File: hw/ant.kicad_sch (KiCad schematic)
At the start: 0 parts

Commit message: Checkpoint
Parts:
- added J701: Conn_Coaxial_Power, Connector_Coaxial:SMA_Amphenol_132289_EdgeMount, symbol Connector:Conn_Coaxial_Power
- added K701: G5Q-1, Relay_THT:Relay_SPDT_Omron-G5Q-1, symbol Relay:G5Q-1
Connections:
- net AntRx: now also K701.4
- net AntTx: now also K701.3
- new net: J701.1 (In), K701.2
- new net GND: J701.2 (Ext), K701.5
- new net TxRelay: K701.1
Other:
- removed sheet BPF1
- removed sheet BPF10
- removed sheet BPF2
- removed sheet BPF3
- removed sheet BPF4
- removed sheet BPF5
- removed sheet BPF6
- removed sheet BPF7
- removed sheet BPF8
- removed sheet BPF9
- title: Antenna Tuner, BPF Array, Tx/Rx Relays -> Antenna Tuner, Tx/Rx Relays

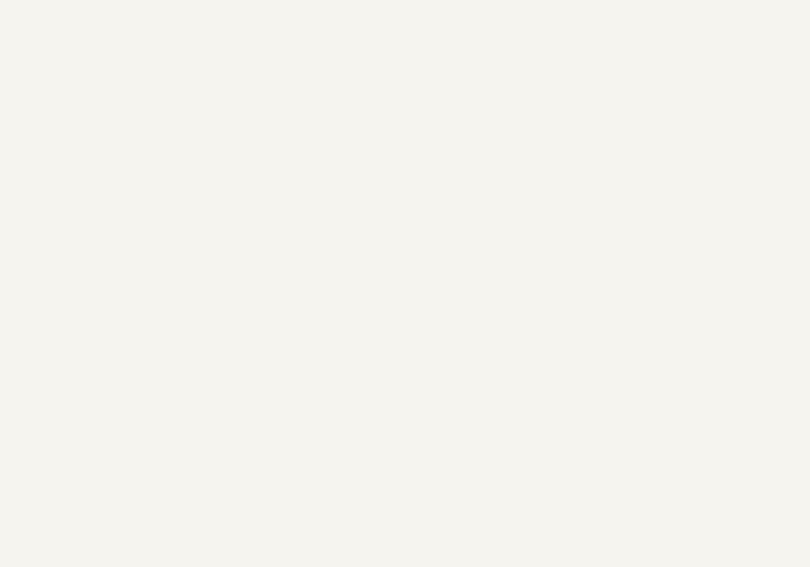
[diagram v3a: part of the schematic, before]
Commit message: Starting to switch to new rx architecture
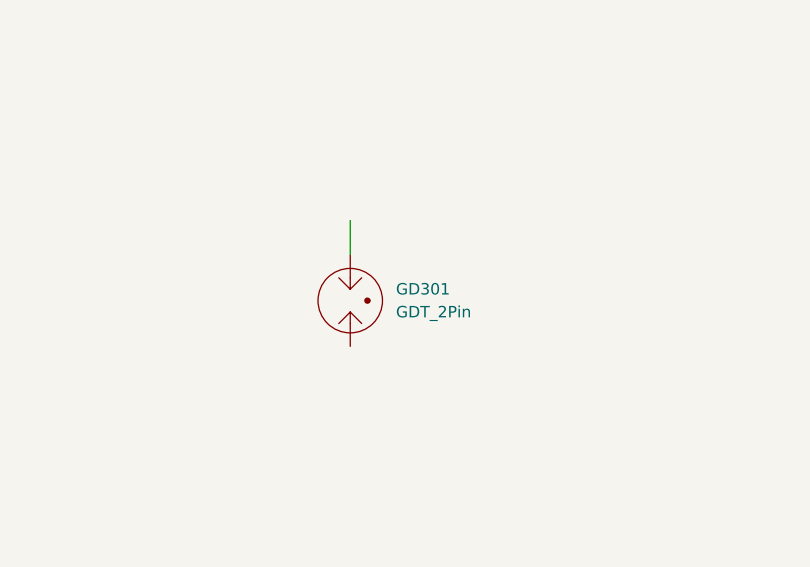
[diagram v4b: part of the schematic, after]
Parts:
- added GD301: GDT_2Pin, symbol Device:GDT_2Pin
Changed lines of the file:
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@@
+		)
+	)
+	(wire
+		(pts
+			(xy 114.3 76.2) (xy 114.3 72.39)
+		)
+		(stroke
+			(width 0)
+			(type default)
 		)
 	)
@@
 					(unit 1)
 				)
+			)
+		)
+	)
+	(symbol
+		(lib_id "Device:GDT_2Pin")
+		(at 114.3 81.28 0)
+		(unit 1)
+		(exclude_from_sim no)
+		(in_bom yes)
+		(on_board yes)
+		(dnp no)
+		(fields_autoplaced yes)
+		(property "Reference" "GD301"
+			(at 119.38 80.0099 0)
+			(effects
+				(font
+					(size 1.27 1.27)
+				)
+				(justify left)
+			)
+		)
+		(property "Value" "GDT_2Pin"
+			(at 119.38 82.5499 0)
+			(effects
+				(font
+					(size 1.27 1.27)
+				)
+				(justify left)
+			)
+		)
+		(property "Footprint" ""
+			(at 114.3 81.28 90)
+			(effects
+				(font
+					(size 1.27 1.27)
+				)
+				(hide yes)
+			)
+		)
+		(property "Datasheet" "~"
+			(at 114.3 81.28 90)
+			(effects
+				(font
+					(size 1.27 1.27)
+				)
+				(hide yes)
+			)
+		)
+		(property "Description" "Gas Discharge Tube with 2 Pins"
+			(at 114.3 81.28 0)
+			(effects
+				(font
+					(size 1.27 1.27)
+				)
+				(hide yes)
+			)
+		)
+		(pin "3"
+		)
+		(pin "1"
+		)
+		(instances
+			(project "USB-SSB-txcvr"
+				(path "/8ae46c04-d01a-4756-8774-512b694bfaff/1ffb1160-1891-4fab-821d-83a4f4ddba5b"
+					(reference "GD301")
+					(unit 1)
+				)

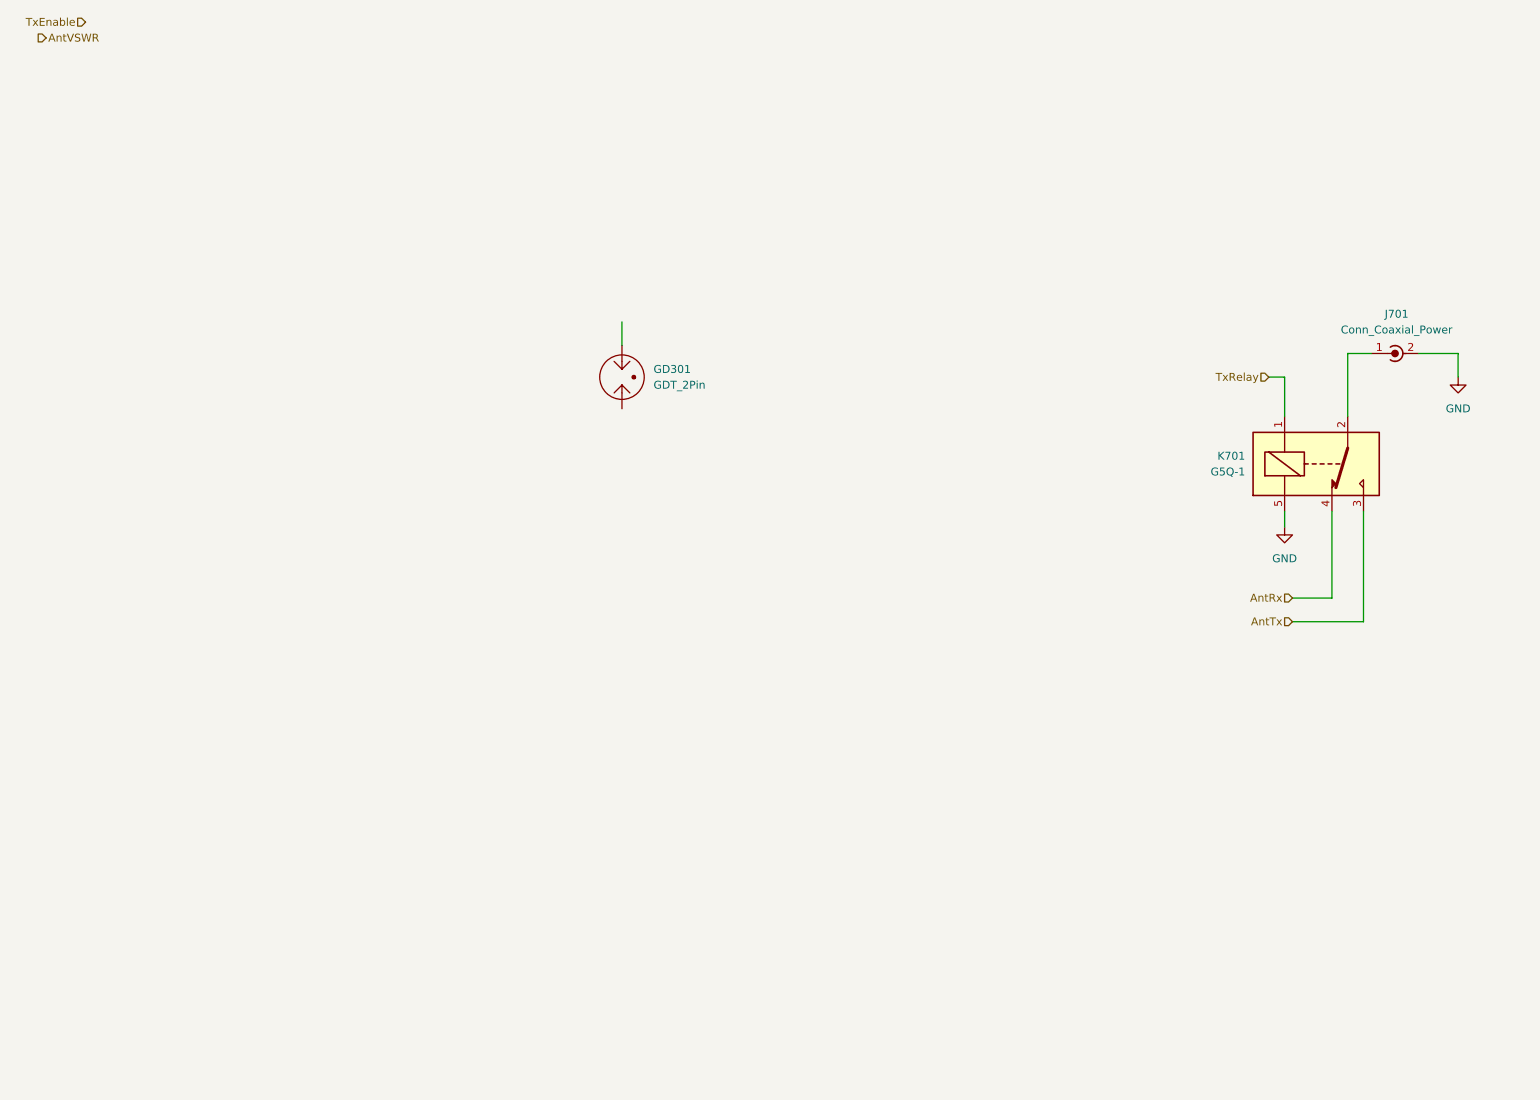
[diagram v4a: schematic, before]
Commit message: Converting to use busses as global symbols instead of tedium. Using 2n7002 Nexperia dual MOSFET because of its LOW LOW capacitance spec for L, C, and attenuator switching.
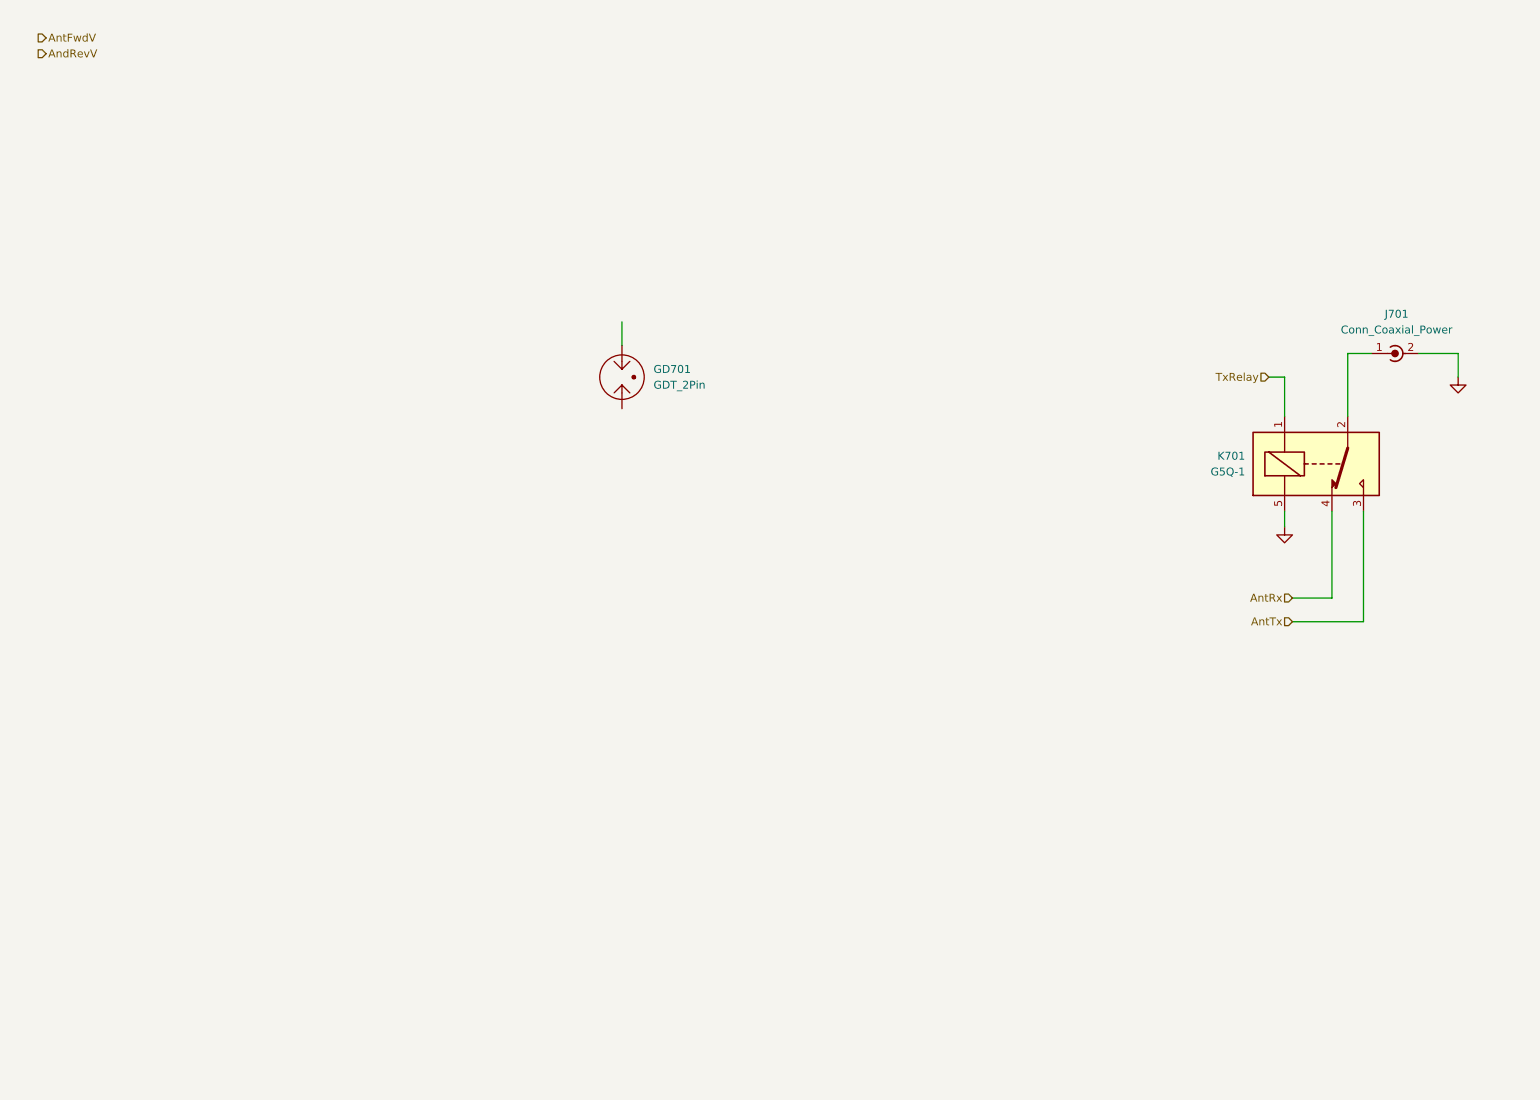
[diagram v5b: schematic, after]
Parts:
- renumbered GD301 to GD701
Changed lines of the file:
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@@
 		)
 	)
-	(hierarchical_label "TxEnable"
-		(shape input)
-		(at 27.94 24.13 180)
+	(hierarchical_label "AntFwdV"
+		(shape output)
+		(at 20.32 26.67 0)
 		(effects
 			(font
 				(size 1.27 1.27)
 			)
-			(justify right)
-		)
-	)
-	(hierarchical_label "AntVSWR"
+			(justify left)
+		)
+	)
+	(hierarchical_label "AndRevV"
 		(shape output)
-		(at 20.32 26.67 0)
+		(at 20.32 29.21 0)
 		(effects
 			(font
@@
 					(size 1.27 1.27)
 				)
+				(hide yes)
 			)
 		)
@@
 					(size 1.27 1.27)
 				)
+				(hide yes)
 			)
 		)
@@
 		(dnp no)
 		(fields_autoplaced yes)
-		(property "Reference" "GD301"
+		(property "Reference" "GD701"
 			(at 119.38 80.0099 0)
 			(effects
@@
 			(project "USB-SSB-txcvr"
 				(path "/8ae46c04-d01a-4756-8774-512b694bfaff/1ffb1160-1891-4fab-821d-83a4f4ddba5b"
-					(reference "GD301")
+					(reference "GD701")
 					(unit 1)
 				)

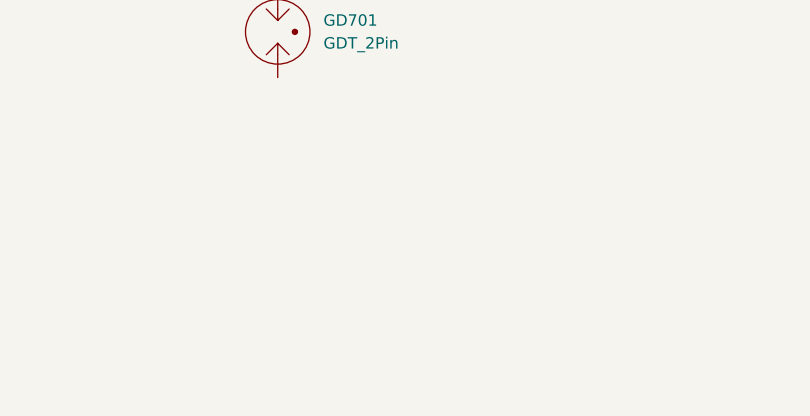
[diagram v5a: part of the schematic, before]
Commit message: LC tank for tx side is now switch C + switch L using reed relays. Rx preselector in flux but coming together
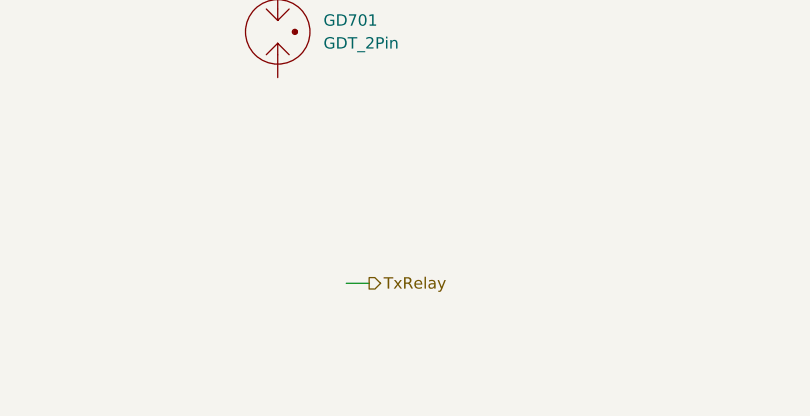
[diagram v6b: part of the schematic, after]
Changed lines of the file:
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@@
+		)
+	)
+	(wire
+		(pts
+			(xy 121.92 109.22) (xy 124.46 109.22)
+		)
+		(stroke
+			(width 0)
+			(type default)
 		)
 	)
@@
 		)
 	)
+	(hierarchical_label "TxRelay"
+		(shape output)
+		(at 124.46 109.22 0)
+		(effects
+			(font
+				(size 1.27 1.27)
+			)
+			(justify left)
+		)
+	)

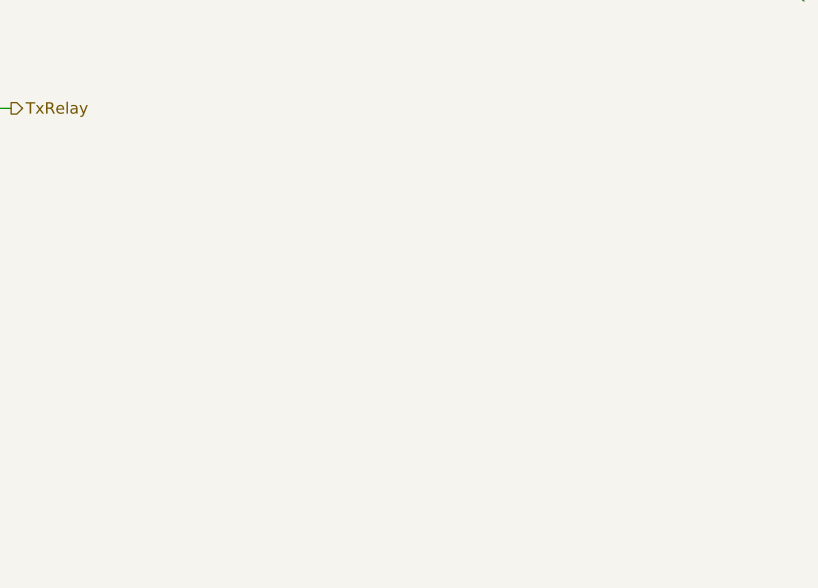
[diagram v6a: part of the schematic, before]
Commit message: More Tx LPF design and a doc. The schematic now reflects 200 ohm domain for the LPFs and the PA LC tanks too.
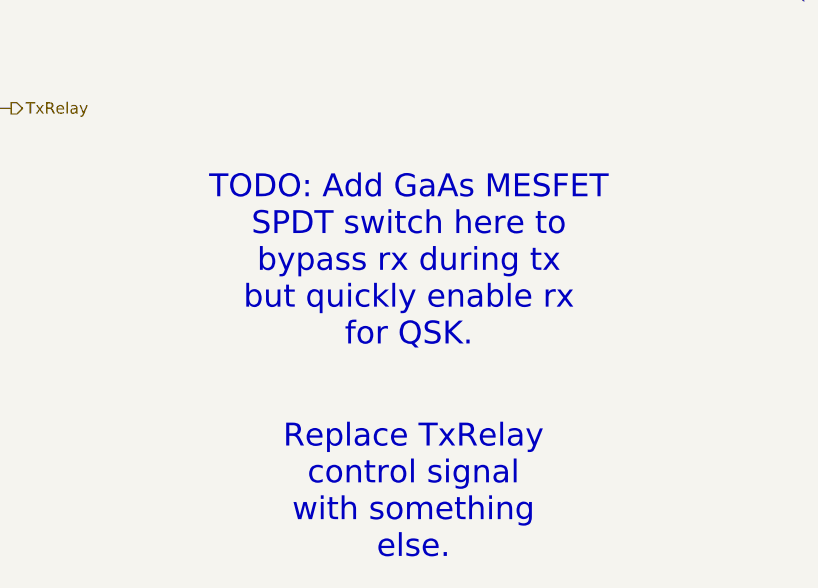
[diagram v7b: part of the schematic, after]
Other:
- note added: "Replace TxRelay control signal with something else."
- note added: "TODO: Add GaAs MESFET SPDT switch here to bypass rx during tx but quickly enable rx for QSK."
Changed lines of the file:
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@@
 		(comment 1 "Alan Mimms")
+	)
+	(text "TODO: Add GaAs MESFET\nSPDT switch here to\nbypass rx during tx\nbut quickly enable rx\nfor QSK."
+		(exclude_from_sim no)
+		(at 168.656 126.238 0)
+		(effects
+			(font
+				(size 2.54 2.54)
+			)
+		)
+	)
+	(text "Replace TxRelay\ncontrol signal\nwith something\nelse."
+		(exclude_from_sim no)
+		(at 169.164 151.892 0)
+		(effects
+			(font
+				(size 2.54 2.54)
+			)
+		)
 	)
 	(wire
